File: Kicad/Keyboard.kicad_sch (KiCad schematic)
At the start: 28 parts, among them J1 USB_C_Receptacle_USB2.0_16P, J2 Conn_01x04, SW71 RotaryEncoder_Switch, U1 ATmega32U4-A, U2 USB6B1, Y1 Crystal_GND24_Small

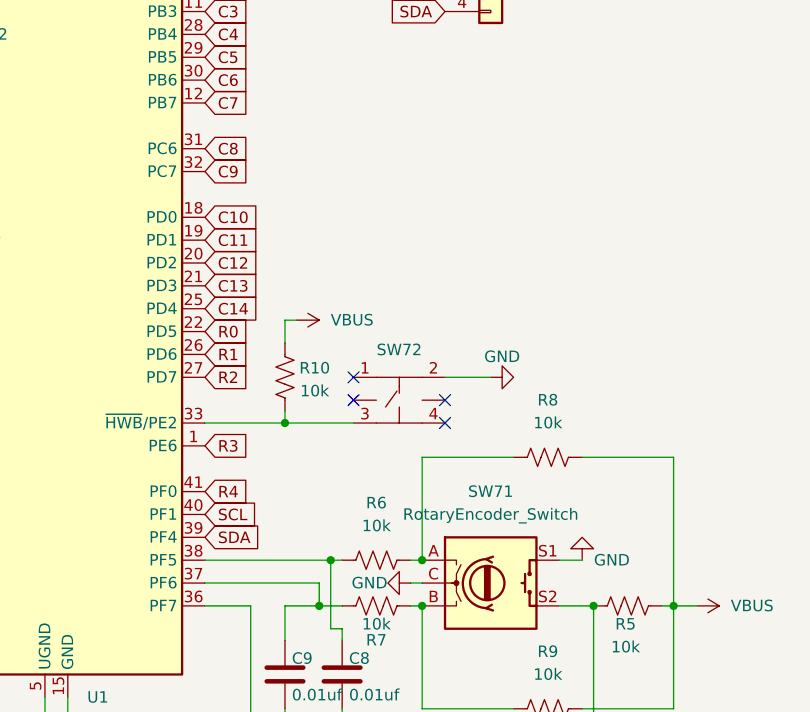
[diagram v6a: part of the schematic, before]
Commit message: caught huge mcu i2c issue
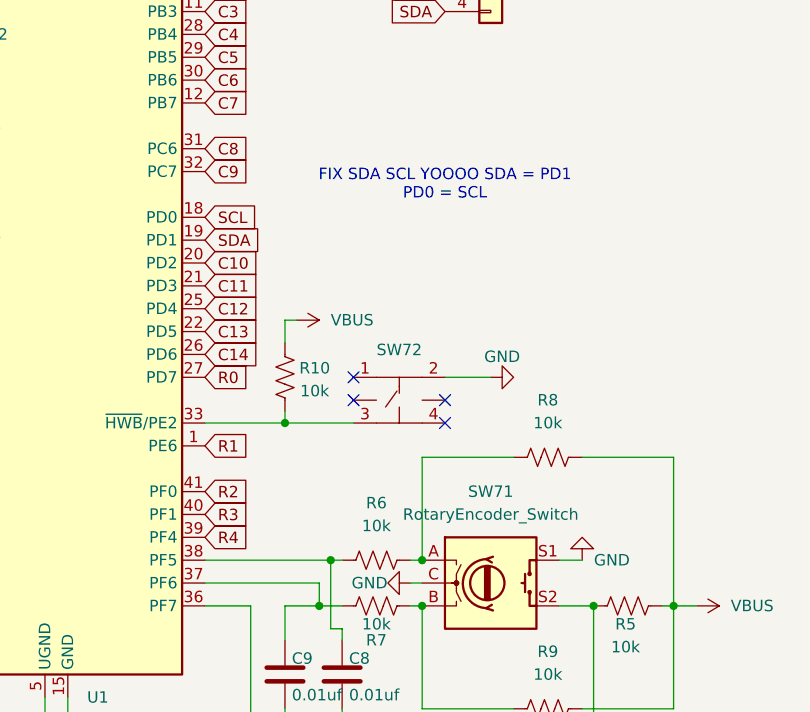
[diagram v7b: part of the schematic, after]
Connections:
- net C10: now also U1.20 (PD2); no longer U1.18 (PD0)
- net C11: now also U1.21 (PD3); no longer U1.19 (PD1)
- net C12: now also U1.25 (PD4); no longer U1.20 (PD2)
- net C13: now also U1.22 (PD5); no longer U1.21 (PD3)
- net C14: now also U1.26 (PD6); no longer U1.25 (PD4)
- net R0: now also U1.27 (PD7); no longer U1.22 (PD5)
- net R1: now also U1.1 (PE6); no longer U1.26 (PD6)
- net R2: now also U1.41 (PF0); no longer U1.27 (PD7)
- net R3: now also U1.40 (PF1); no longer U1.1 (PE6)
- net R4: now also U1.39 (PF4); no longer U1.41 (PF0)
- net SCL: now also U1.18 (PD0); no longer U1.40 (PF1)
- net SDA: now also U1.19 (PD1); no longer U1.39 (PF4)
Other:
- note added: "FIX SDA SCL YOOOO SDA = PD1 PD0 = SCL"

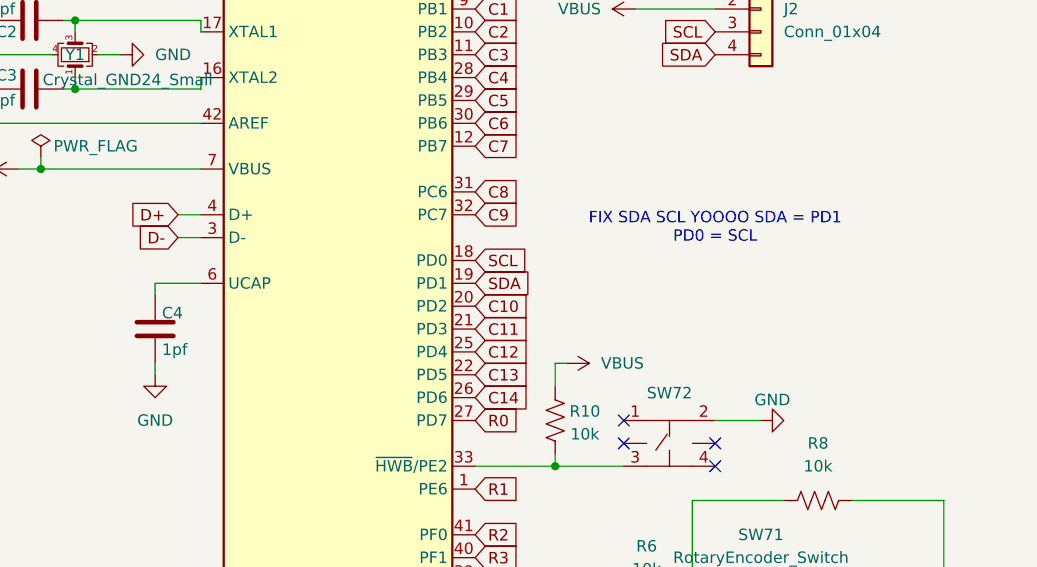
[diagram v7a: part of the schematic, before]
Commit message: stitching vias
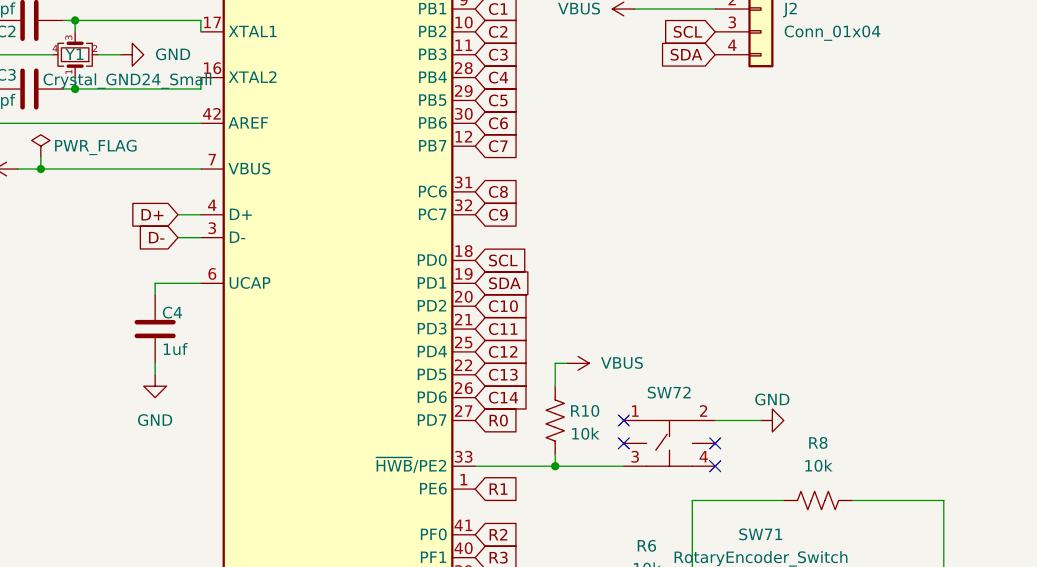
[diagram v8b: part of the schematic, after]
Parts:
- C4: value 1pf -> 1uf
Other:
- note removed: "FIX SDA SCL YOOOO SDA = PD1 PD0 = SCL"
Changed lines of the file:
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@@
 		(comment 1 "65% keyboard")
 	)
-	(text "FIX SDA SCL YOOOO SDA = PD1 \nPD0 = SCL "
-		(exclude_from_sim no)
-		(at 104.14 65.024 0)
-		(effects
-			(font
-				(size 1.27 1.27)
-			)
-		)
-	)
 	(junction
 		(at 53.34 29.21)
@@
 			)
 		)
-		(property "Value" "1pf"
+		(property "Value" "1uf"
 			(at 42.672 78.486 0)
 			(effects
